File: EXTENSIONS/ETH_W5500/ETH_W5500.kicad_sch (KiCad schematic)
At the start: 69 parts, among them J1 EXT, J2 WE-634008137521, J3 MM-690367290876, U2 AP1117-33, U3 W5500, Y1 25M

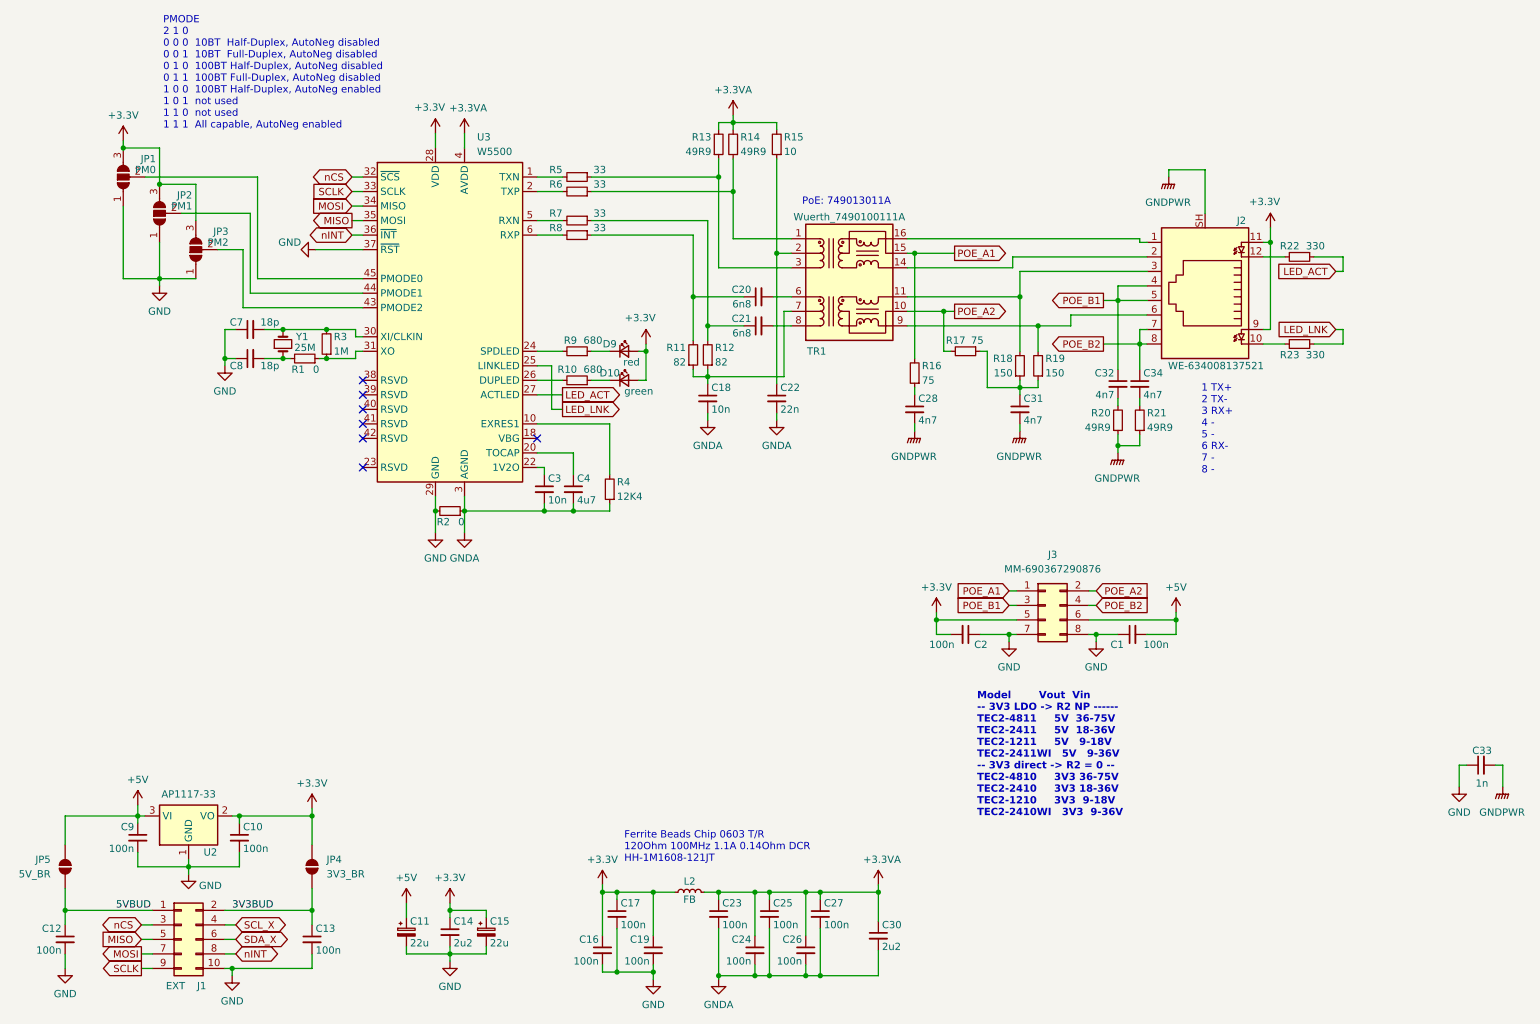
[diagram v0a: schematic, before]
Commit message: Improve documentation and ETH-Extension
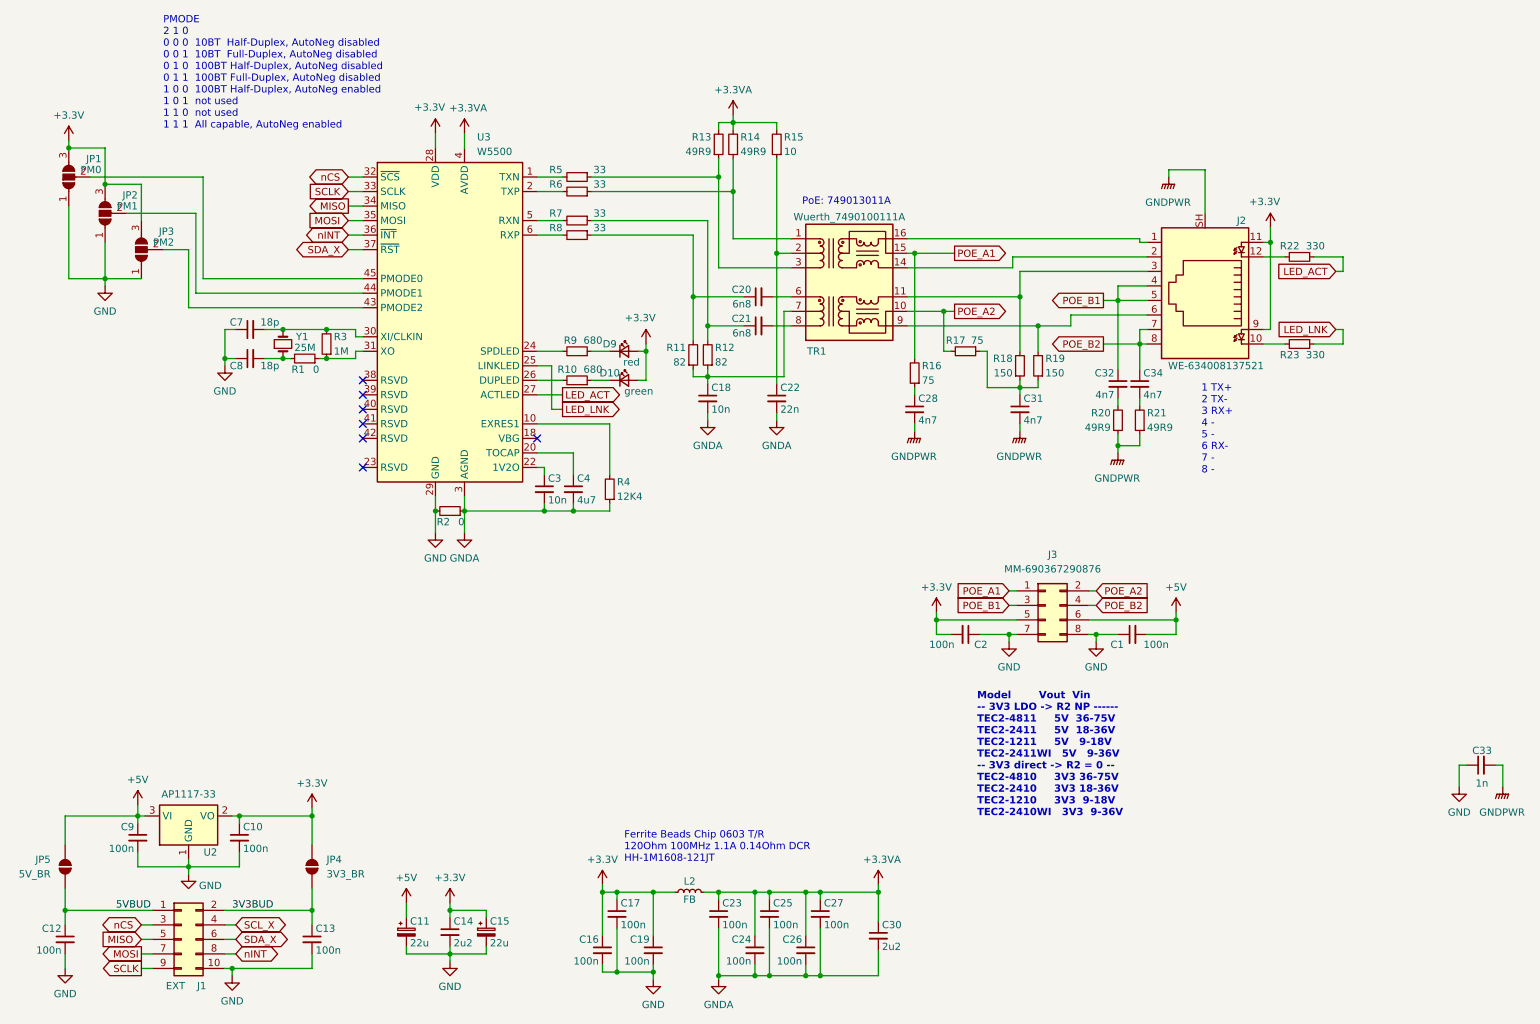
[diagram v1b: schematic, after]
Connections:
- net GND: no longer U3.37 (~{RST})
- net MISO: now also U3.34 (MISO); no longer U3.35 (MOSI)
- net MOSI: now also U3.35 (MOSI); no longer U3.34 (MISO)
- net SDA_X: now also U3.37 (~{RST})
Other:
- moved on the sheet: JP1, JP2, JP3

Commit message: Page settings use project text variables.
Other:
- company: the78mole -> ${COMPANY}
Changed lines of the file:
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@@
 	(title_block
 		(title "KM271-WiFi-ETHext")
-		(date "2025-01-13")
-		(rev "0.0.3")
-		(company "the78mole")
-		(comment 1 "Author: Daniel Glaser")
+		(date "${CREATION_DATE}")
+		(rev "${REVISION}")
+		(company "${COMPANY}")
+		(comment 1 "Author: ${AUTHOR}")
 	)
 	(text "PMODE\n2 1 0  \n0 0 0  10BT  Half-Duplex, AutoNeg disabled\n0 0 1  10BT  Full-Duplex, AutoNeg disabled\n0 1 0  100BT Half-Duplex, AutoNeg disabled\n0 1 1  100BT Full-Duplex, AutoNeg disabled\n1 0 0  100BT Half-Duplex, AutoNeg enabled\n1 0 1  not used\n1 1 0  not used\n1 1 1  All capable, AutoNeg enabled"
